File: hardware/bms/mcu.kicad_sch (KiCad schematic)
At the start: 53 parts, among them SW2 SW_Push, SW3 SW_Push, U4 LM5166X, U5 TPS62172DSG, U6 ESP32-C3-MINI-1-N4, U7 SN74LXC1T14DCKR

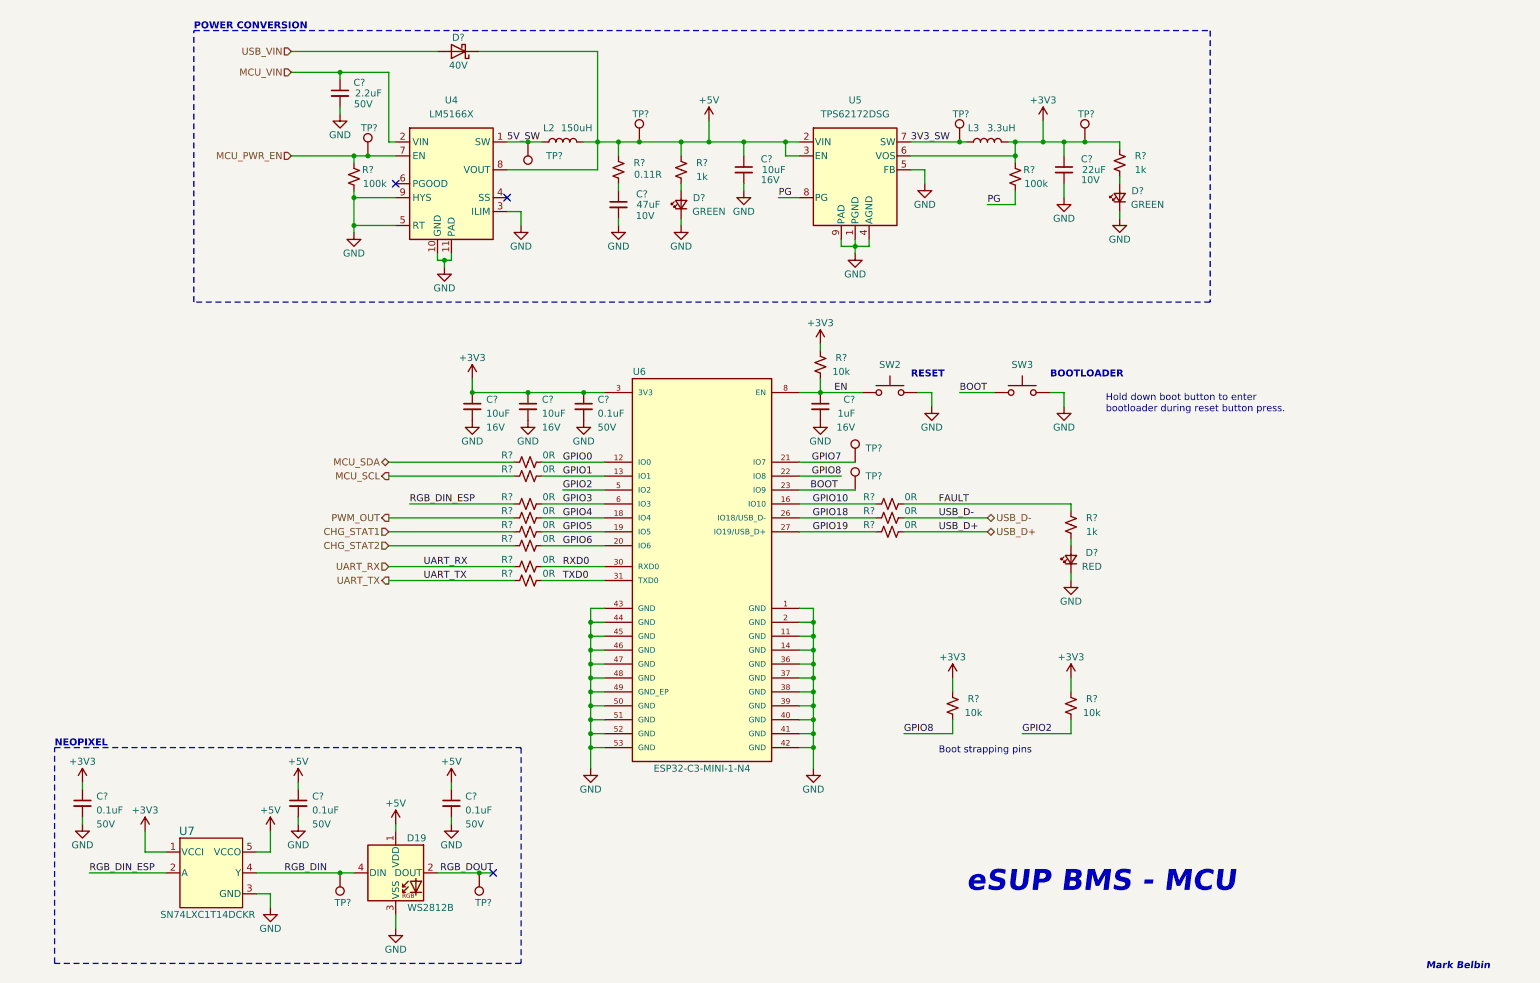
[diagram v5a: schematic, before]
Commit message: Added Micro SD card circuit.
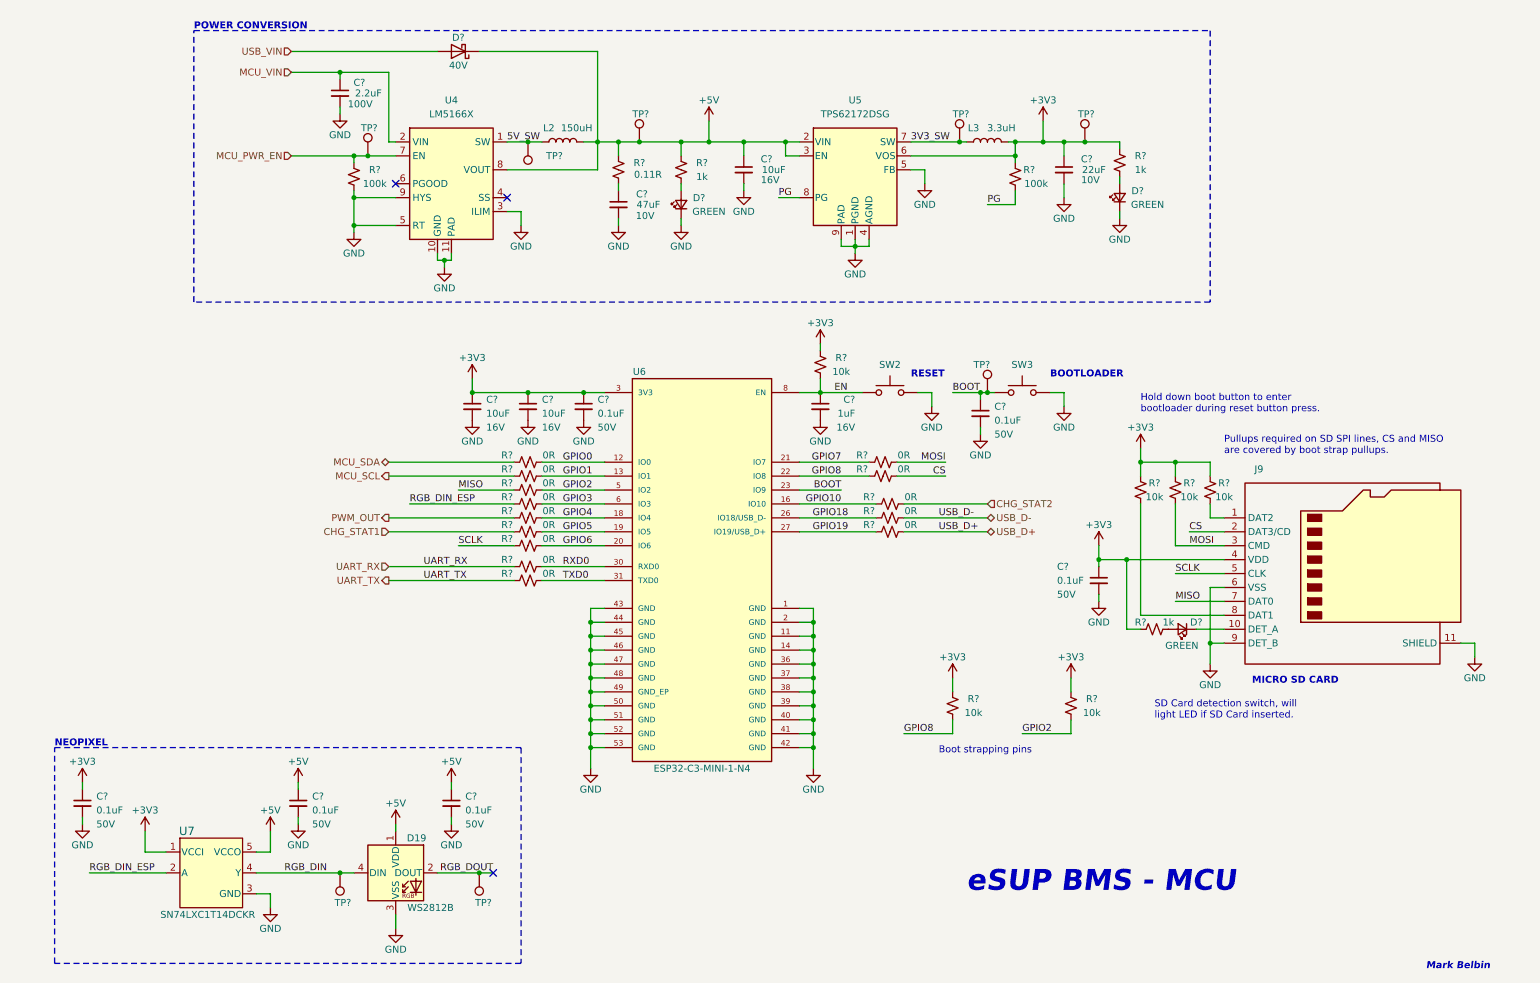
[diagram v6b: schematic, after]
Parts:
- removed D?: RED, LED_SMD:LED_0603_1608Metric, symbol Device:LED_Small
- removed R?: 0R, Resistor_SMD:R_0603_1608Metric, symbol Device:R_Small_US
- removed R?: 1k, Resistor_SMD:R_0603_1608Metric, symbol Device:R_Small_US
- removed TP?: TestPoint, bms:TestPoint_Pad_D0.5mm, symbol Connector:TestPoint
- added C? (x2): 0.1uF, Capacitor_SMD:C_0603_1608Metric, symbol Device:C_Small
- added D?: GREEN, LED_SMD:LED_0603_1608Metric, symbol Device:LED_Small
- added J9: Micro_SD_Card_Det2, bms:microSD_HC_Molex_104031-0811, symbol Connector:Micro_SD_Card_Det2
- added R? (x4): 0R, Resistor_SMD:R_0603_1608Metric, symbol Device:R_Small_US
- added R? (x3): 10k, Resistor_SMD:R_0603_1608Metric, symbol Device:R_Small_US
- added R?: 1k, Resistor_SMD:R_0603_1608Metric, symbol Device:R_Small_US
- C?: footprint Capacitor_SMD:C_1206_3216Metric -> Capacitor_SMD:C_1210_3225Metric; MFG Murata Electronics -> Taiyo Yuden; MFG PN GCM31CR71H225KA55L -> HMK325B7225KM-P; Voltage 50V -> 100V
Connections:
- net +3V3: now also C?.1, J9.4 (VDD), R?.1, R?.1, R?.1, R?.2
- net BOOT: now also C?.1
- net CHG_STAT2: now also R?.2; no longer R?.1
- net GND: now also C?.2, C?.2, J9.11 (SHIELD), J9.6 (VSS), J9.9 (DET_B)
- net GPIO10: now also R?.1
- net GPIO2: now also R?.2
- net GPIO7: now also R?.1
- net GPIO8: now also R?.1
- new net: D?.1 (K), J9.10 (DET_A)
- new net: D?.2 (A), R?.1
- new net: J9.8 (DAT1), R?.2
- new net: J9.1 (DAT2), R?.2
- new net CS: J9.2 (DAT3/CD), R?.2
- new net MISO: J9.7 (DAT0), R?.1
- new net MOSI: J9.3 (CMD), R?.2, R?.2
- new net SCLK: J9.5 (CLK), R?.1
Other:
- note added: "MICRO SD CARD"
- note added: "Pullups required on SD SPI lines, CS and MISO are covered by boot strap pullups."
- note added: "SD Card detection switch, will light LED if SD Card inserted."
- moved on the sheet: TP?

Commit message: Added extra features to try and prevent SD card data corruption. Added override enable so that the MCU can keep itself on until the SD card is finished writing, also added 5V / wake detect circuit so the MCU can begin to sense when the 5V rail is dropping and react accordingly
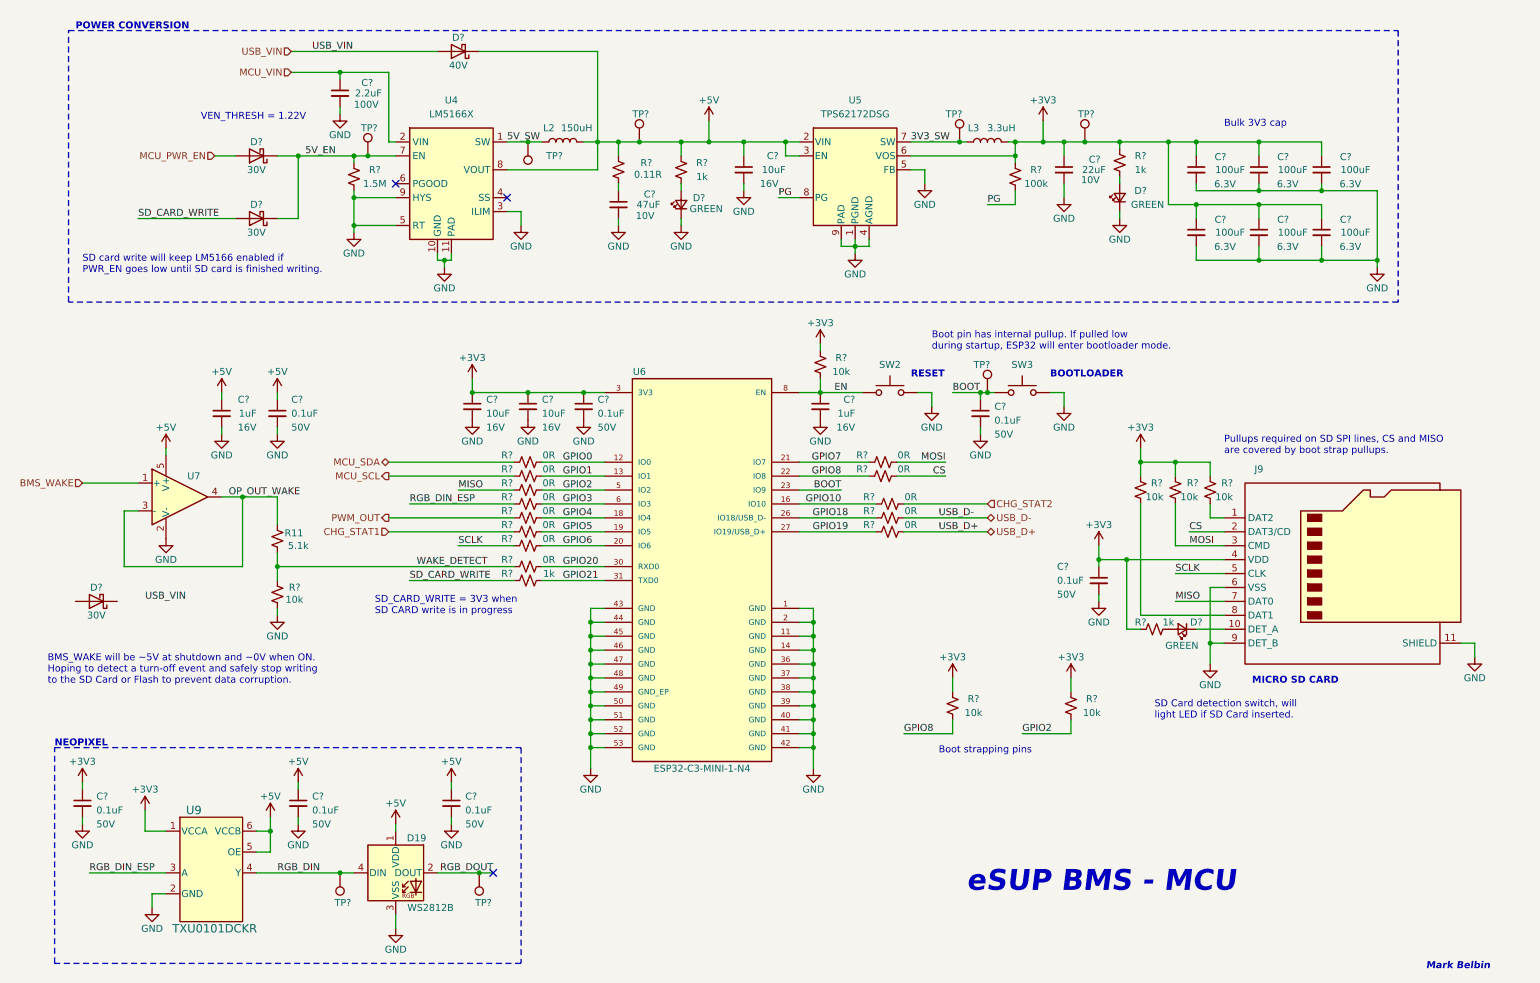
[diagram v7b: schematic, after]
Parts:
- removed R?: 0R, Resistor_SMD:R_0603_1608Metric, symbol Device:R_Small_US
- removed U7: SN74LXC1T14DCKR, bms:DCK0005A-IPC_C, symbol bms:SN74LXC1T14DCKR
- added C? (x6): 100uF, Capacitor_SMD:C_1210_3225Metric, symbol Device:C_Small
- added C?: 1uF, Capacitor_SMD:C_0603_1608Metric, symbol Device:C_Small
- added C?: 0.1uF, Capacitor_SMD:C_0603_1608Metric, symbol Device:C_Small
- added D? (x3): D_Schottky, Diode_SMD:D_SOD-123, symbol Device:D_Schottky
- added R11: 5.1k, Resistor_SMD:R_0603_1608Metric, symbol Device:R_Small_US
- added R?: 10k, Resistor_SMD:R_0603_1608Metric, symbol Device:R_Small_US
- added R?: 1k, Resistor_SMD:R_0603_1608Metric, symbol Device:R_Small_US
- added U7: MCP6001U, Package_TO_SOT_SMD:SOT-23-5, symbol Amplifier_Operational:MCP6001U
- added U9: TXU0101DCKR, Package_TO_SOT_SMD:SOT-363_SC-70-6, symbol bms:TXU0101DCKR
- R?: value 100k -> 1.5M; MFG PN ERJ-3EKF1003V -> ERJ-3GEYJ155V
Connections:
- net +3V3: now also C?.1, C?.1, C?.1, C?.1, C?.1, C?.1, U9.1 (VCCA)
- net +5V: now also C?.1, C?.1, U7.5 (V+), U9.5 (OE), U9.6 (VCCB)
- net GND: now also C?.2, C?.2, C?.2, C?.2, C?.2, C?.2, C?.2, C?.2, R?.2, U7.2 (V-), U9.2 (GND)
- net MCU_PWR_EN: now also D?.2 (A); no longer R?.2, TP?.1, U4.7 (EN)
- net RGB_DIN: now also U9.4 (Y)
- net RGB_DIN_ESP: now also U9.3 (A)
- net RXD0 renamed GPIO20
- net TXD0 renamed GPIO21
- net GPIO21: now also R?.1
- net UART_RX renamed WAKE_DETECT
- net WAKE_DETECT: now also R11.1, R?.1
- new net 5V_EN: D?.1 (K), D?.1 (K), R?.2, TP?.1, U4.7 (EN)
- new net BMS_WAKE: U7.1 (+)
- new net OP_OUT_WAKE: R11.2, U7.3 (-), U7.4
- new net SD_CARD_WRITE: D?.2 (A), R?.2
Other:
- note added: "BMS_WAKE will be ~5V at shutdown and ~0V when ON. Hoping to detect a turn-off event and safely stop writing to the SD Card or Flash to prevent data corruption."
- note added: "Boot pin has internal pullup. If pulled low during startup, ESP32 will enter bootloader mode."
- note added: "Bulk 3V3 cap"
- note added: "SD card write will keep LM5166 enabled if PWR_EN goes low until SD card is finished writing."
- note added: "SD_CARD_WRITE = 3V3 when SD CARD write is in progress"
- note added: "VEN_THRESH = 1.22V"
- note removed: "Hold down boot button to enter bootloader during reset button press."

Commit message: Added bulk cap for 5V and 3V3 rails, made sure they fit in current layout
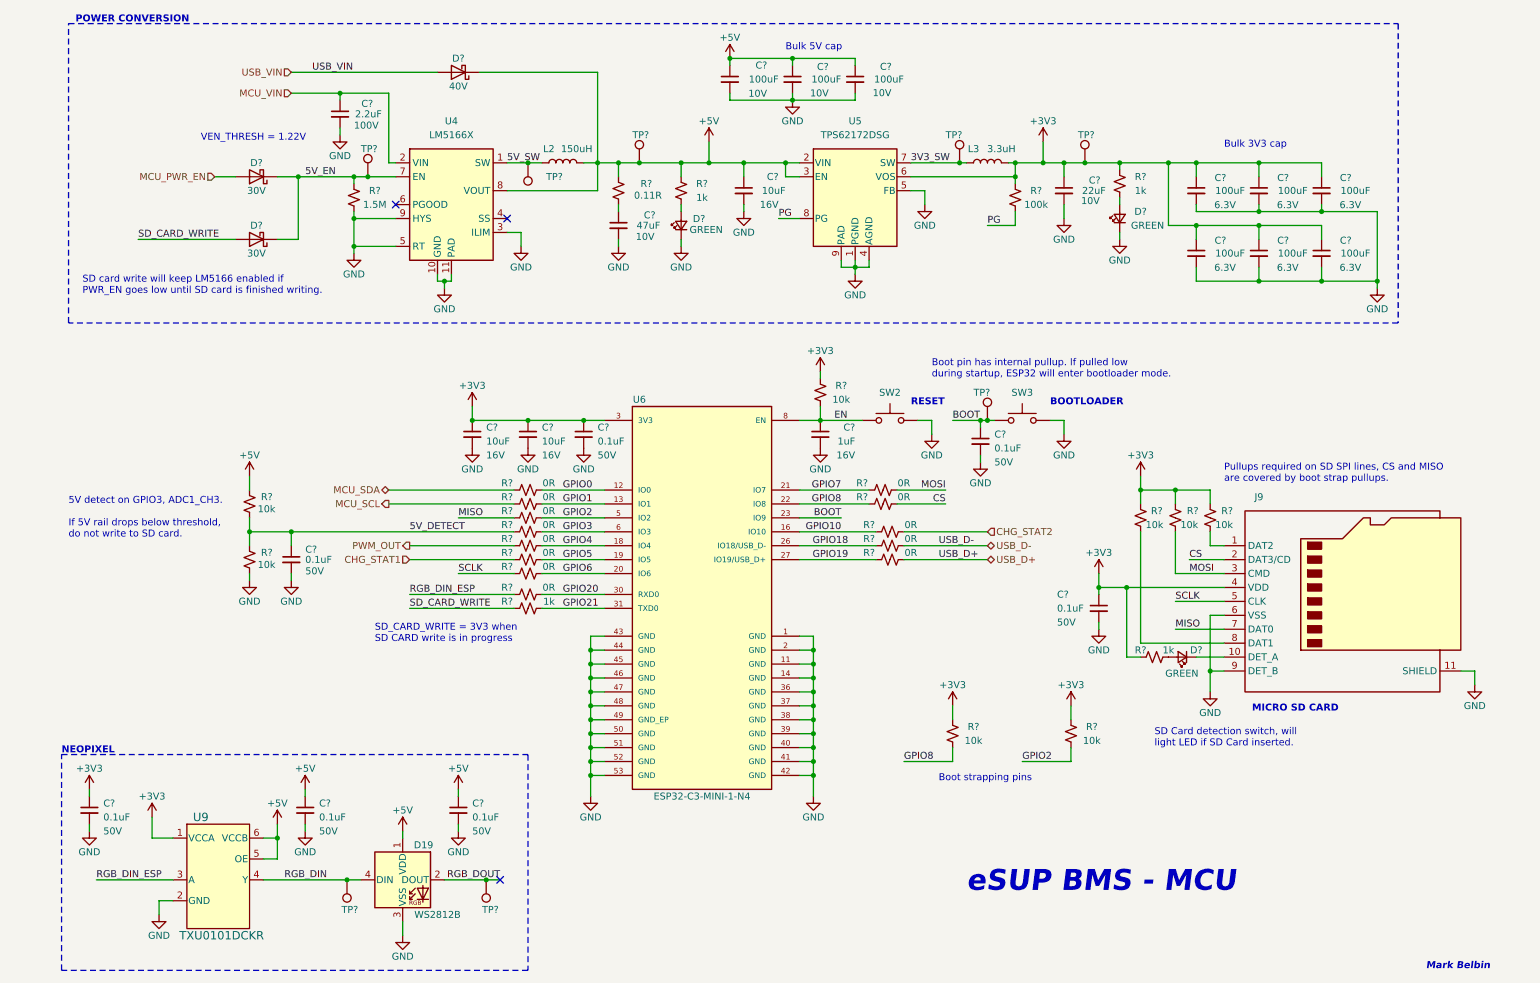
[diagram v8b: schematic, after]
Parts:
- removed C?: 1uF, Capacitor_SMD:C_0603_1608Metric, symbol Device:C_Small
- removed C?: 0.1uF, Capacitor_SMD:C_0603_1608Metric, symbol Device:C_Small
- removed D?: D_Schottky, Diode_SMD:D_SOD-123, symbol Device:D_Schottky
- removed R11: 5.1k, Resistor_SMD:R_0603_1608Metric, symbol Device:R_Small_US
- removed U7: MCP6001U, Package_TO_SOT_SMD:SOT-23-5, symbol Amplifier_Operational:MCP6001U
- added C? (x3): 100uF, Capacitor_SMD:C_1210_3225Metric, symbol Device:C_Small
- added C?: 0.1uF, Capacitor_SMD:C_0603_1608Metric, symbol Device:C_Small
- added R?: 10k, Resistor_SMD:R_0603_1608Metric, symbol Device:R_Small_US
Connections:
- net +5V: now also C?.1, C?.1, C?.1, R?.1
- net GND: now also C?.2, C?.2, C?.2, C?.2
- net RGB_DIN_ESP: now also R?.1; no longer R?.1
- net WAKE_DETECT renamed 5V_DETECT
- net 5V_DETECT: now also R?.1, C?.1, R?.2; no longer R?.1
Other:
- note added: "5V detect on GPIO3, ADC1_CH3. If 5V rail drops below threshold, do not write to SD card."
- note added: "Bulk 5V cap"
- note removed: "BMS_WAKE will be ~5V at shutdown and ~0V when ON. Hoping to detect a turn-off event and safely stop writing to the SD Card or Flash to prevent data corruption."
- moved on the sheet: C?, D19, D?, J9, L2, L3, R?, SW2, SW3, TP?, U4, U5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
